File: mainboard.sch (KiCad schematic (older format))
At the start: 73 parts, among them J1 Conn_01x06, J2 USB_B_Micro, J3 xf2m-2415-1a, J4 XF2M-1015-1A, J5 Conn_01x02, J6 U.FL-R-SMT-1, J7 Conn_02x02_Top_Bottom, Q1 RADFET, SW1 KMR231NG LFS, U1 BMX160, U11 AP2112K-3.3, U2 MAX708RESA-T, U3 ATSAMD51J20A-M, U4 DRV8830DRC, U5 MR25H40, U6 DRV8830DRC, U7 ADS124S06IRHBR, U8 DRV8830DRC, U9 RFM98PW-symbols

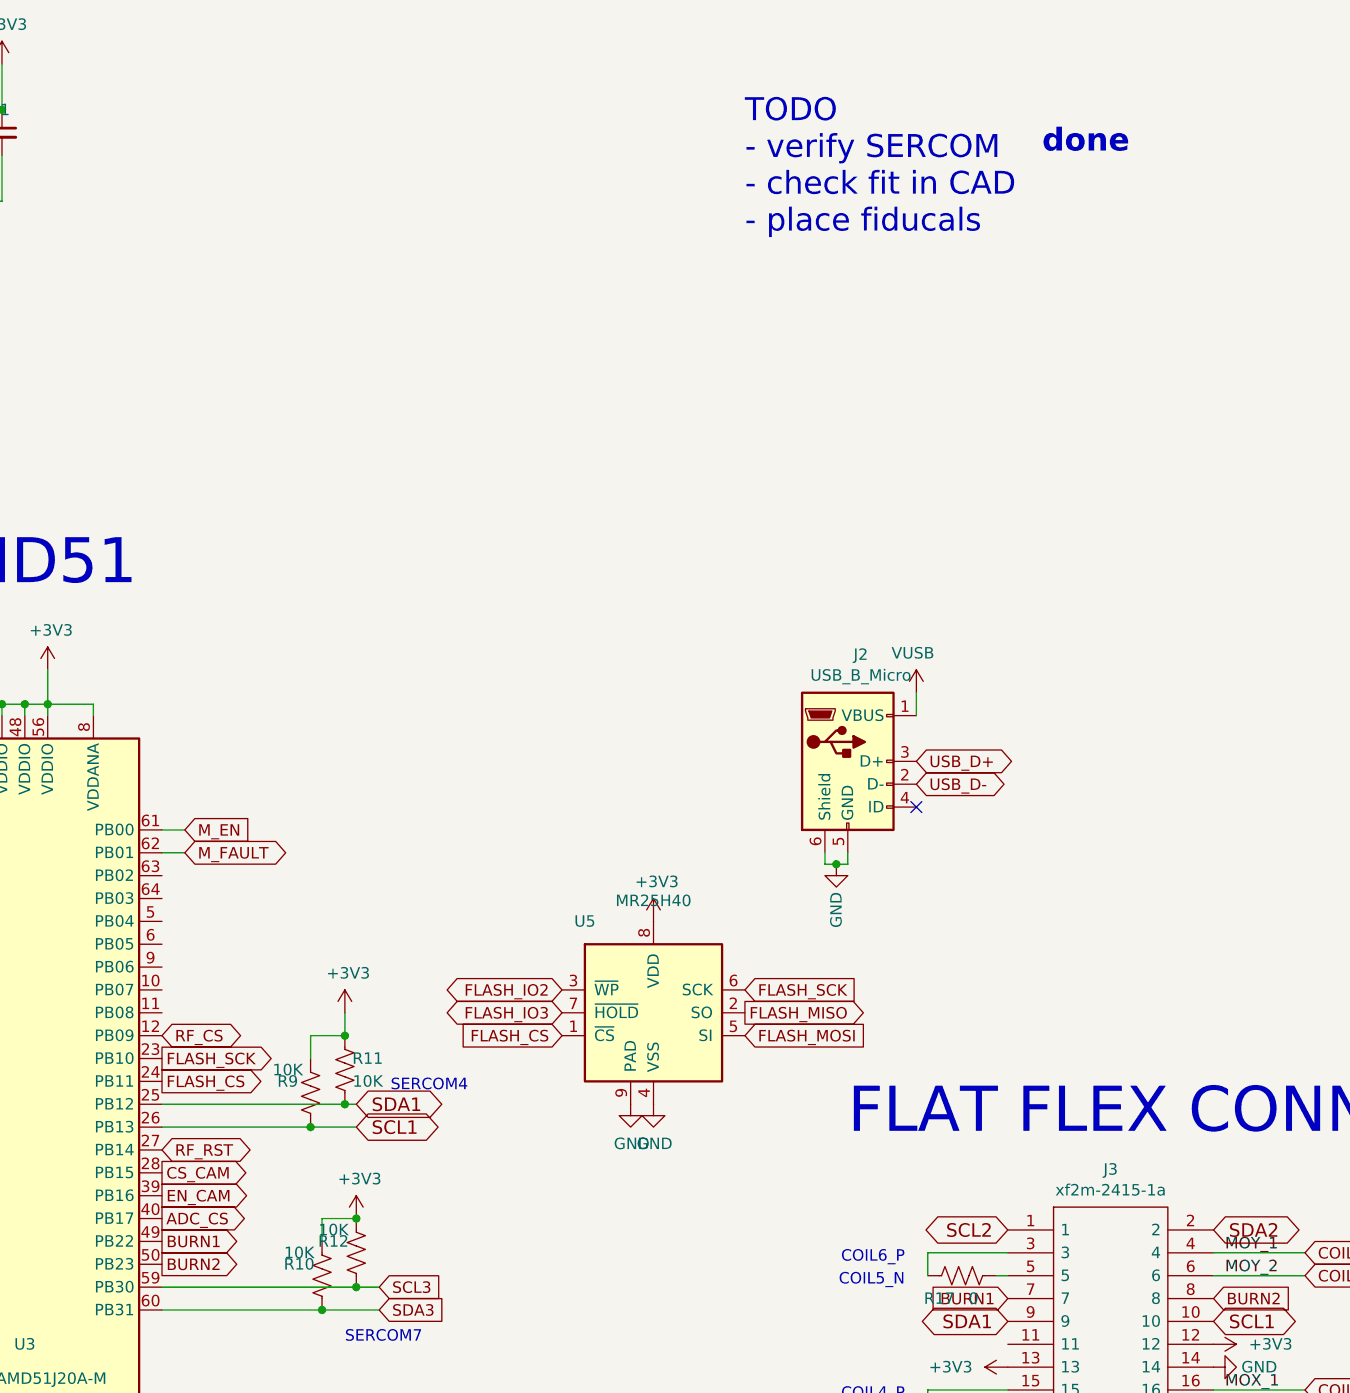
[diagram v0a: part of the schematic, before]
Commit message: fit-checked with CAD
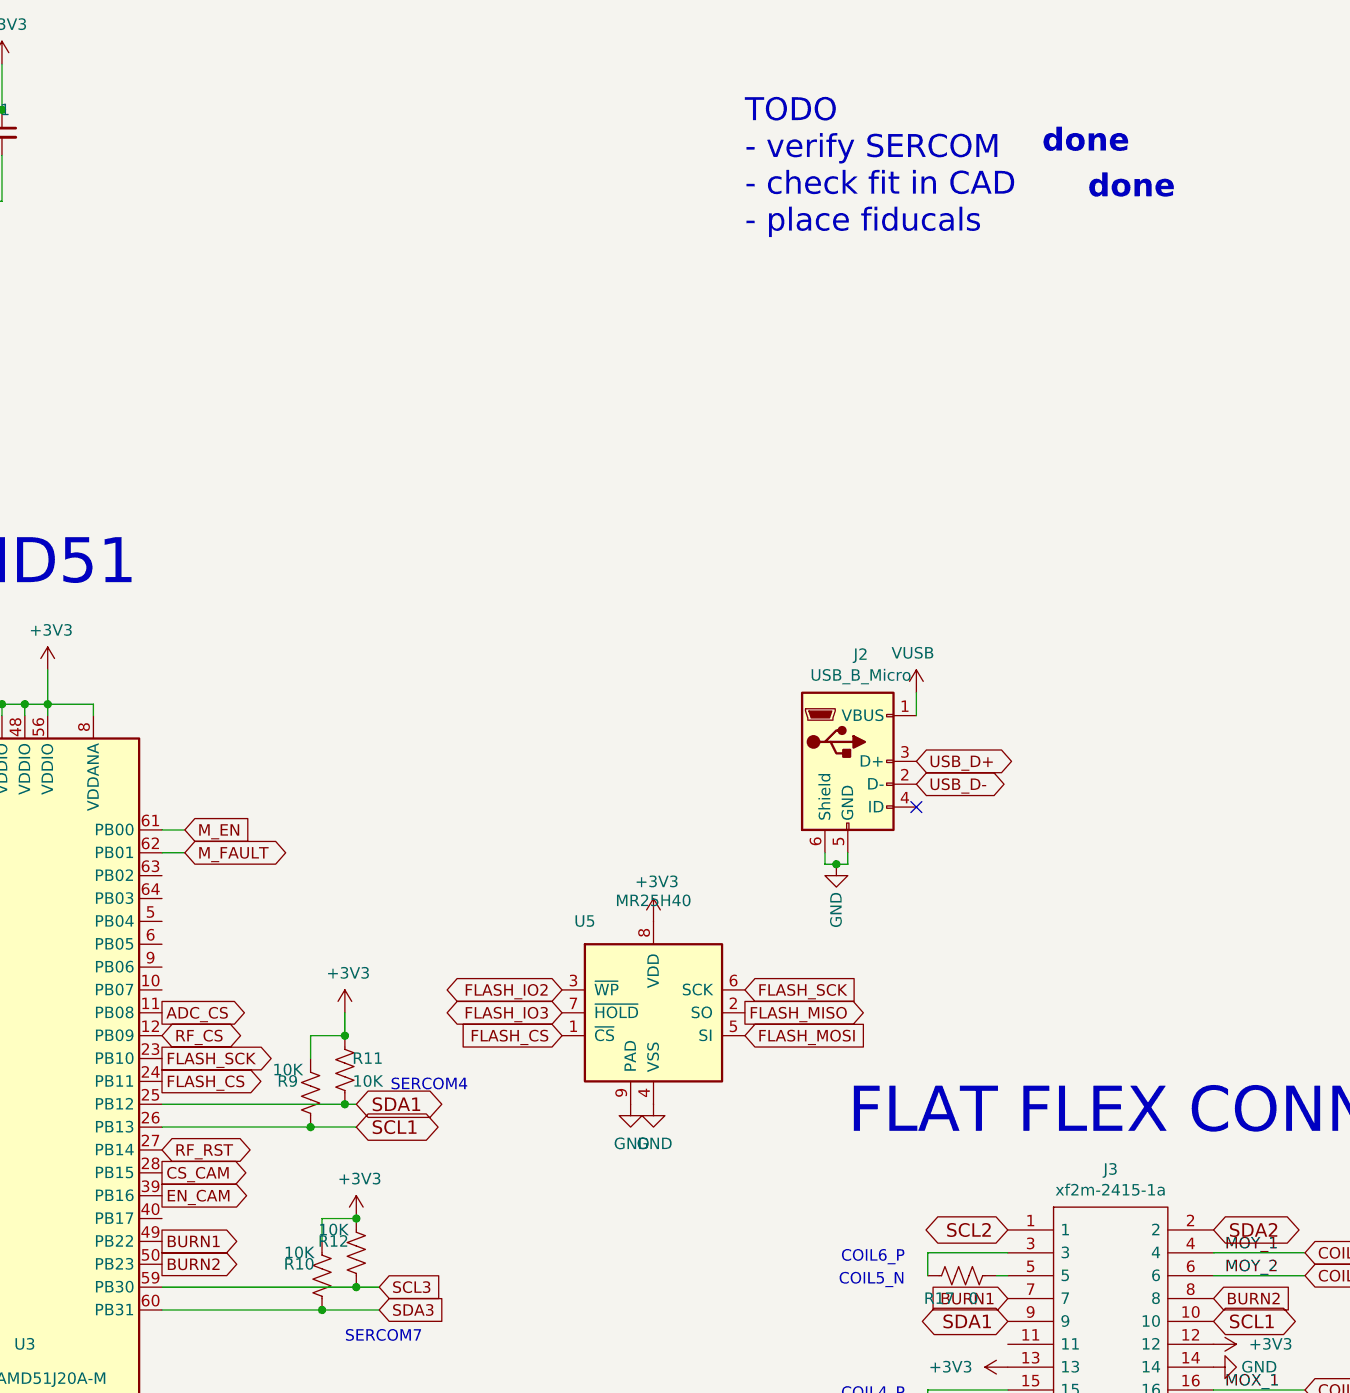
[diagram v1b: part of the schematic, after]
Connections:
- net ADC_CS: now also U3.11 (PB08); no longer U3.40 (PB17)

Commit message: removed dosimeter & roughed in new RBF header
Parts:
- removed C14, C20: 1uF, Capacitor_SMD:C_0402_1005Metric, symbol mainboard-rescue:C_Small-Device
- removed C15, C16: 0.1uF, Capacitor_SMD:C_0402_1005Metric, symbol mainboard-rescue:C_Small-Device
- removed Q1: RADFET, Package_TO_SOT_SMD:SOT-23-6, symbol mainboard-rescue:RADFET-symbols
- removed R22, R24: 10K, Resistor_SMD:R_0402_1005Metric, symbol mainboard-rescue:R_US-Device
- removed U7: ADS124S06IRHBR, custom-footprints:ADS124208_withpad, symbol mainboard-rescue:ADS124S06IRHBR-symbols
- J7: footprint Connector_PinSocket_1.27mm:PinSocket_2x02_P1.27mm_Vertical_SMD -> Connector_PinHeader_1.27mm:PinHeader_2x02_P1.27mm_Horizontal
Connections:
- net +3V3: now also J7.3 (Pin_3); no longer J7.1 (Pin_1)
- net BATT_P: now also J7.2 (Pin_2); no longer J7.3 (Pin_3)
- net GND: now also J7.1 (Pin_1); no longer J7.4 (Pin_4)
- net at C19.1, U11.5 (VOUT): now also J7.4 (Pin_4); no longer J7.2 (Pin_2)
- net ADC_CS: no longer names the net of U3.11 (PB08)
- net ADC_DRDY: no longer names the net of U3.16 (PA07)
- no-connect marks 9 -> 8
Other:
- note removed: "DOSIMETER"
- moved on the sheet: J7

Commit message: roughed-in SD card
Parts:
- added J8: Micro_SD_Card, Connector_Card:microSD_HC_Molex_104031-0811, symbol Connector:Micro_SD_Card
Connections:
- net RF_IO2: no longer names the net of U9.8 (GPIO_2)
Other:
- note added: "TODO\n- verify SERCOM\n- check fit in CAD\n- place fiducals\n- add rbf\n- fit SD maybe?"
- note removed: "TODO\n- verify SERCOM\n- check fit in CAD\n- place fiducals"
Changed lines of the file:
@@
 Text GLabel 14400 5350 0    50   BiDi ~ 0
 RF_IO1
-Text GLabel 15600 4750 2    50   BiDi ~ 0
-RF_IO2
 Wire Wire Line
 	15600 4650 15600 4400
@@
 	0    -1   -1   0
 $EndComp
-Text Notes 6400 4400 0    100  ~ 0
-TODO\n- verify SERCOM\n- check fit in CAD\n- place fiducals
-Text Notes 7700 4050 0    100  ~ 20
+Text Notes 7750 3750 0    100  ~ 20
 done
 Text GLabel 14400 5250 0    50   BiDi ~ 0
@@
 Text GLabel 2450 7400 0    50   BiDi ~ 0
 RF_IO0
-Text Notes 7900 4250 0    100  ~ 20
+Text Notes 7900 3950 0    100  ~ 20
 done
 Wire Wire Line
@@
 	-1   0    0    -1
 $EndComp
+$Comp
+L Connector:Micro_SD_Card J8
+U 1 1 5F583739
+P 14100 6600
+F 0 "J8" H 14050 7317 50  0000 C CNN
+F 1 "Micro_SD_Card" H 14050 7226 50  0000 C CNN
+F 2 "Connector_Card:microSD_HC_Molex_104031-0811" H 15250 6900 50  0001 C CNN
+F 3 "http://katalog.we-online.de/em/datasheet/693072010801.pdf" H 14100 6600 50  0001 C CNN
+	1    14100 6600
+	1    0    0    -1
+$EndComp
+Text Notes 6400 4400 0    100  ~ 0
+TODO\n- verify SERCOM\n- check fit in CAD\n- place fiducals\n- add rbf\n- fit SD maybe?
 $EndSCHEMATC

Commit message: routed
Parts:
- TP1, TP2: footprint TestPoint:TestPoint_Keystone_5015_Micro-Minature -> TestPoint:TestPoint_Pad_1.0x1.0mm
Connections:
- net +3V3: now also J8.4 (VDD)
- net GND: now also J8.6 (VSS), J8.9 (SHIELD)
- net MISO: now also J8.7 (DAT0)
- net MOSI: now also J8.3 (CMD)
- net M_FAULT: now also U3.27 (PB14); no longer U3.62 (PB01)
- net RF_CS: now also U3.43 (PA22); no longer U3.12 (PB09)
- net RF_RST: now also U3.41 (PA20); no longer U3.27 (PB14)
- net SCK: now also J8.5 (CLK)
- net SD_CS: now reaches U3.11 (PB08)
- net SD_CS: now also J8.2 (DAT3/CD)
- no-connect marks 8 -> 10
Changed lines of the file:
@@
 	1    0    0    -1
 $EndComp
-Text GLabel 3850 7900 2    50   BiDi ~ 0
-RF_CS
 Text GLabel 2450 7300 0    50   BiDi ~ 0
 RF_IO1
-Text GLabel 3850 8400 2    50   BiDi ~ 0
+Text GLabel 2450 8900 0    50   BiDi ~ 0
 RF_RST
 $Comp
@@
 Text GLabel 1350 7200 0    50   Input ~ 0
 BATT_P
-Text GLabel 3950 7100 2    50   BiDi ~ 0
-M_FAULT
 Text GLabel 3850 8800 2    50   Output ~ 0
 BURN1
@@
 F 0 "TP1" H 10158 9918 50  0000 L CNN
 F 1 "TestPoint" H 10158 9827 50  0000 L CNN
-F 2 "TestPoint:TestPoint_Keystone_5015_Micro-Minature" H 10300 9800 50  0001 C CNN
+F 2 "TestPoint:TestPoint_Pad_1.0x1.0mm" H 10300 9800 50  0001 C CNN
 F 3 "~" H 10300 9800 50  0001 C CNN
 	1    10100 9800
@@
 F 0 "TP2" H 10608 9918 50  0000 L CNN
 F 1 "TestPoint" H 10608 9827 50  0000 L CNN
-F 2 "TestPoint:TestPoint_Keystone_5015_Micro-Minature" H 10750 9800 50  0001 C CNN
+F 2 "TestPoint:TestPoint_Pad_1.0x1.0mm" H 10750 9800 50  0001 C CNN
 F 3 "~" H 10750 9800 50  0001 C CNN
 	1    10550 9800
@@
 Wire Wire Line
 	3850 7000 3950 7000
-Wire Wire Line
-	3850 7100 3950 7100
 Text GLabel 2450 7700 0    50   Output ~ 0
 FLASH_MOSI
@@
 Text Notes 6400 4400 0    100  ~ 0
 TODO\n- verify SERCOM\n- check fit in CAD\n- place fiducals\n- add rbf\n- fit SD maybe?
+Text GLabel 13200 6700 0    59   Input ~ 0
+SCK
+Text GLabel 13200 6500 0    59   Input ~ 0
+MOSI
+Text GLabel 13200 6900 0    59   Output ~ 0
+MISO
+Text GLabel 13200 6400 0    59   Input ~ 0
+SD_CS
+NoConn ~ 13200 7000
+NoConn ~ 13200 6300
+$Comp
+L power:GND #PWR0109
+U 1 1 5F636FAE
+P 14900 7200
+F 0 "#PWR0109" H 14900 6950 50  0001 C CNN
+F 1 "GND" H 14905 7027 50  0000 C CNN
+F 2 "" H 14900 7200 50  0001 C CNN
+F 3 "" H 14900 7200 50  0001 C CNN
+	1    14900 7200
+	1    0    0    -1
+$EndComp
+$Comp
+L power:GND #PWR0110
+U 1 1 5F637458
+P 12950 6800
+F 0 "#PWR0110" H 12950 6550 50  0001 C CNN
+F 1 "GND" V 12955 6672 50  0000 R CNN
+F 2 "" H 12950 6800 50  0001 C CNN
+F 3 "" H 12950 6800 50  0001 C CNN
+	1    12950 6800
+	0    1    1    0
+$EndComp
+Wire Wire Line
+	12950 6800 13200 6800
+$Comp
+L power:+3V3 #PWR0111
+U 1 1 5F644092
+P 12950 6600
+F 0 "#PWR0111" H 12950 6450 50  0001 C CNN
+F 1 "+3V3" V 12965 6728 50  0000 L CNN
+F 2 "" H 12950 6600 50  0001 C CNN
+F 3 "" H 12950 6600 50  0001 C CNN
+	1    12950 6600
+	0    -1   -1   0
+$EndComp
+Wire Wire Line
+	12950 6600 13200 6600
+Text GLabel 3850 7800 2    59   Output ~ 0
+SD_CS
+Text GLabel 3850 8400 2    50   BiDi ~ 0
+M_FAULT
+Text GLabel 2450 9100 0    50   BiDi ~ 0
+RF_CS
 $EndSCHEMATC

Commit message: added xtal
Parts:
- added C14, C15: 10pF, Capacitor_SMD:C_0402_1005Metric, symbol mainboard-rescue:C_Small-Device
- added Y1: Crystal, Crystal:Crystal_SMD_3215-2Pin_3.2x1.5mm, symbol Device:Crystal
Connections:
- net GND: now also C14.1, C15.2
- net at U3.1 (PA00): now also C14.2, Y1.1
- net at U3.2 (PA01): now also C15.1, Y1.2
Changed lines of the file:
@@
 Text GLabel 2450 9100 0    50   BiDi ~ 0
 RF_CS
+$Comp
+L Device:Crystal Y1
+U 1 1 5F84E26C
+P 2050 6850
+F 0 "Y1" V 2004 6981 50  0000 L CNN
+F 1 "Crystal" V 2095 6981 50  0000 L CNN
+F 2 "Crystal:Crystal_SMD_3215-2Pin_3.2x1.5mm" H 2050 6850 50  0001 C CNN
+F 3 "~" H 2050 6850 50  0001 C CNN
+	1    2050 6850
+	0    1    1    0
+$EndComp
+$Comp
+L mainboard-rescue:C_Small-Device C14
+U 1 1 5F84FE74
+P 1700 6750
+F 0 "C14" V 1929 6750 50  0000 C CNN
+F 1 "10pF" V 1838 6750 50  0000 C CNN
+F 2 "Capacitor_SMD:C_0402_1005Metric" H 1700 6750 50  0001 C CNN
+F 3 "~" H 1700 6750 50  0001 C CNN
+	1    1700 6750
+	0    -1   -1   0
+$EndComp
+$Comp
+L mainboard-rescue:C_Small-Device C15
+U 1 1 5F850793
+P 1700 6950
+F 0 "C15" V 1837 6950 50  0000 C CNN
+F 1 "10pF" V 1928 6950 50  0000 C CNN
+F 2 "Capacitor_SMD:C_0402_1005Metric" H 1700 6950 50  0001 C CNN
+F 3 "~" H 1700 6950 50  0001 C CNN
+	1    1700 6950
+	0    1    1    0
+$EndComp
+Wire Wire Line
+	1800 6750 1900 6750
+Wire Wire Line
+	1900 6750 1900 6700
+Wire Wire Line
+	1900 6700 2050 6700
+Wire Wire Line
+	1800 6950 1900 6950
+Wire Wire Line
+	1900 6950 1900 7000
+Wire Wire Line
+	1900 7000 2050 7000
+Wire Wire Line
+	2450 6900 2350 6900
+Wire Wire Line
+	2350 6900 2350 6700
+Wire Wire Line
+	2350 6700 2050 6700
+Connection ~ 2050 6700
+Wire Wire Line
+	2450 7000 2050 7000
+Connection ~ 2050 7000
+Wire Wire Line
+	1600 6750 1600 6850
+$Comp
+L power:GND #PWR04
+U 1 1 5F8B8A3D
+P 1450 6850
+F 0 "#PWR04" H 1450 6600 50  0001 C CNN
+F 1 "GND" H 1455 6677 50  0000 C CNN
+F 2 "" H 1450 6850 50  0001 C CNN
+F 3 "" H 1450 6850 50  0001 C CNN
+	1    1450 6850
+	1    0    0    -1
+$EndComp
+Wire Wire Line
+	1450 6850 1600 6850
+Connection ~ 1600 6850
+Wire Wire Line
+	1600 6850 1600 6950
 $EndSCHEMATC

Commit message: pretty BOM and schematic pdf
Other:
- note removed: "TODO\n- verify SERCOM\n- check fit in CAD\n- place fiducals\n- add rbf\n- fit SD maybe?"
- note removed: "done"
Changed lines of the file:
@@
 	0    -1   -1   0
 $EndComp
-Text Notes 7750 3750 0    100  ~ 20
-done
 Text GLabel 14400 5250 0    50   BiDi ~ 0
 RF_IO0
 Text GLabel 2450 7400 0    50   BiDi ~ 0
 RF_IO0
-Text Notes 7900 3950 0    100  ~ 20
-done
 Wire Wire Line
 	15600 2100 15400 2100
@@
 	1    0    0    -1
 $EndComp
-Text Notes 6400 4400 0    100  ~ 0
-TODO\n- verify SERCOM\n- check fit in CAD\n- place fiducals\n- add rbf\n- fit SD maybe?
 Text GLabel 13200 6700 0    59   Input ~ 0
 SCK
